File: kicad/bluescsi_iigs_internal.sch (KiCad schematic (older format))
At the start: 26 parts, among them J1 Conn_02x13_Odd_Even, J2 Conn_02x13_Odd_Even, J3 105162-0001, J4 Conn_01x02_Male, J5 Conn_01x02_Male, M1 Screw_Terminal_01x01, M2 Screw_Terminal_01x01, SW1 SW_SPDT, U1 YAAJ_BluePill, U2 UC560x, UCC56xx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

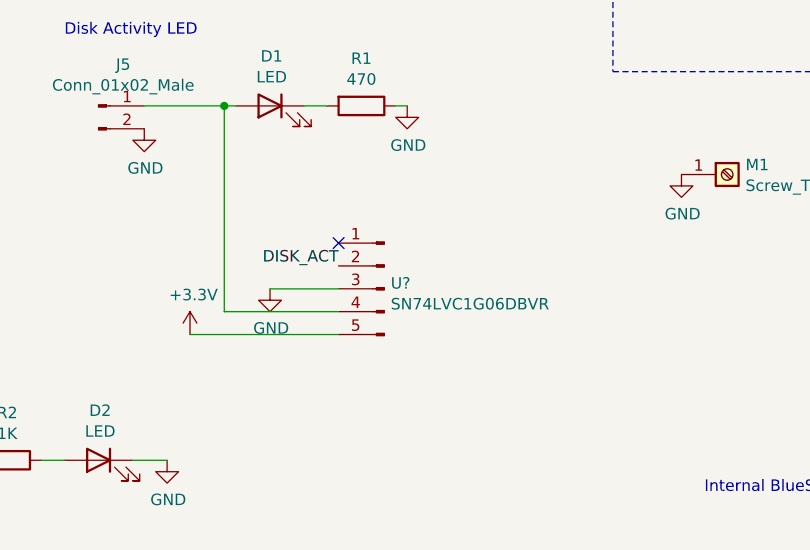
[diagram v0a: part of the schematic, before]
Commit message: Change regulator to back side tab up
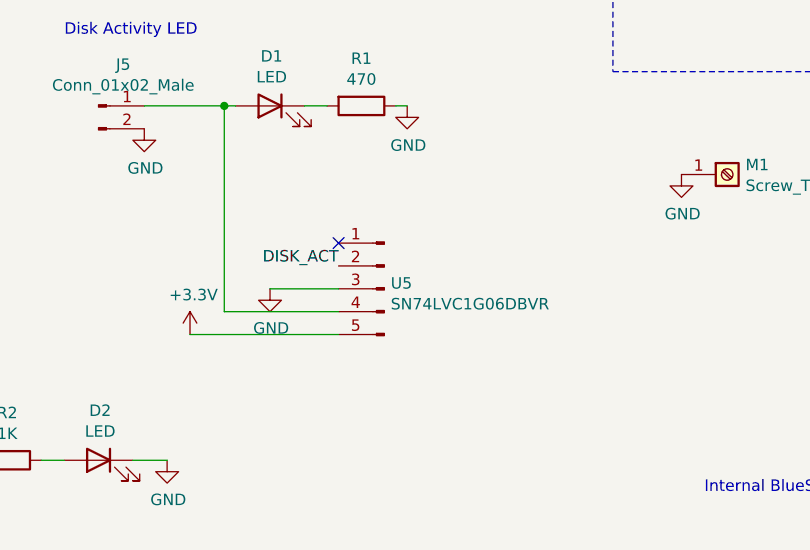
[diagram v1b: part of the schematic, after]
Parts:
- U4: footprint Package_TO_SOT_THT:TO-220-3_Vertical -> Package_TO_SOT_THT:TO-220-3_Horizontal_TabUp
- gave numbers to parts that had none: 1
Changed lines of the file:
@@
 F 0 "U4" H 9300 4842 50  0000 C CNN
 F 1 "MC7805CT-BP" H 9300 4751 50  0000 C CNN
-F 2 "Package_TO_SOT_THT:TO-220-3_Vertical" H 9300 4800 50  0001 C CNN
+F 2 "Package_TO_SOT_THT:TO-220-3_Horizontal_TabUp" H 9300 4800 50  0001 C CNN
 F 3 "https://www.mouser.com/datasheet/2/258/MC7805CT(TO-220)-E-1626349.pdf" H 9400 4350 50  0001 C CNN
 	1    9300 4600
@@
 $EndComp
 $Comp
-L Connector:Conn_01x05_Male U?
+L Connector:Conn_01x05_Male U5
 U 1 1 60C23A85
 P 5950 6600
-F 0 "U?" H 5922 6624 50  0000 R CNN
+F 0 "U5" H 5922 6624 50  0000 R CNN
 F 1 "SN74LVC1G06DBVR" H 5922 6533 50  0000 R CNN
 F 2 "Package_TO_SOT_SMD:SOT-23-5_HandSoldering" H 5950 6600 50  0001 C CNN
@@
 DISK_ACT
 $Comp
-L power:GND #PWR?
+L power:GND #PWR0126
 U 1 1 60C2A0B7
 P 5450 6600
-F 0 "#PWR?" H 5450 6350 50  0001 C CNN
+F 0 "#PWR0126" H 5450 6350 50  0001 C CNN
 F 1 "GND" H 5455 6427 50  0000 C CNN
 F 2 "" H 5450 6600 50  0001 C CNN
@@
 	5750 6600 5450 6600
 $Comp
-L power:+3.3V #PWR?
+L power:+3.3V #PWR0131
 U 1 1 60C2CD62
 P 5100 6800
-F 0 "#PWR?" H 5100 6650 50  0001 C CNN
+F 0 "#PWR0131" H 5100 6650 50  0001 C CNN
 F 1 "+3.3V" H 5115 6973 50  0000 C CNN
 F 2 "" H 5100 6800 50  0001 C CNN

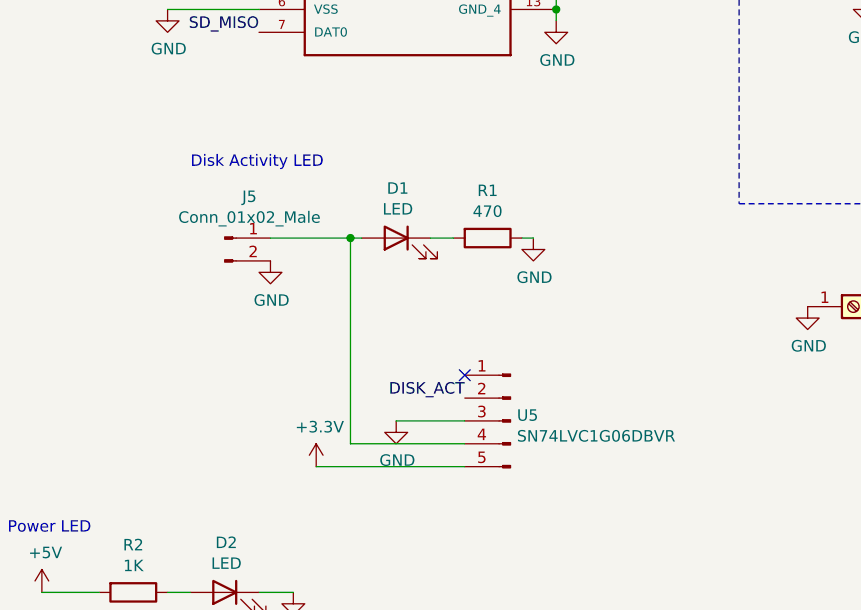
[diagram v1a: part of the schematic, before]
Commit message: Correct LED wiring for active-low with buffer IC
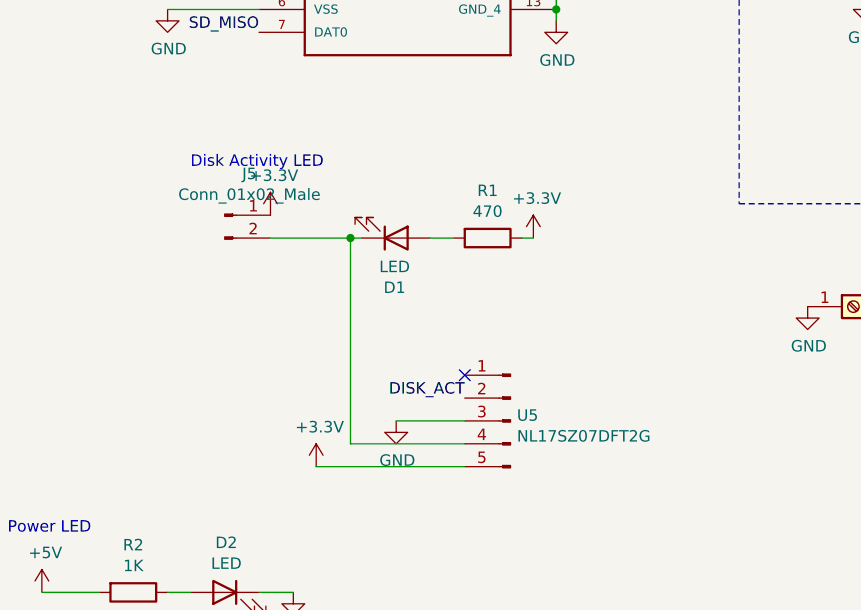
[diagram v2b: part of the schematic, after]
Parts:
- U5: value SN74LVC1G06DBVR -> NL17SZ07DFT2G; footprint Package_TO_SOT_SMD:SOT-23-5_HandSoldering -> Package_TO_SOT_SMD:SOT-353_SC-70-5_Handsoldering
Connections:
- net +3V3: now also J5.1 (Pin_1), R1.1
- net GND: no longer J5.2 (Pin_2), R1.1
- net at D1.1 (K): now also J5.2 (Pin_2), U5.4 (Pin_4); no longer R1.2
- new net: D1.2 (A), R1.2
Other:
- moved on the sheet: D1, J5
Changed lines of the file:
@@
 Wire Wire Line
 	5600 5800 5700 5800
-$Comp
-L power:GND #PWR0127
-U 1 1 609F55CD
-P 6050 5800
-F 0 "#PWR0127" H 6050 5550 50  0001 C CNN
-F 1 "GND" H 6055 5627 50  0000 C CNN
-F 2 "" H 6050 5800 50  0001 C CNN
-F 3 "" H 6050 5800 50  0001 C CNN
-	1    6050 5800
-	1    0    0    -1
-$EndComp
 Wire Wire Line
 	6000 5800 6050 5800
-$Comp
-L Connector:Conn_01x02_Male J5
-U 1 1 60AA760E
-P 4700 5800
-F 0 "J5" H 4808 5981 50  0000 C CNN
-F 1 "Conn_01x02_Male" H 4808 5890 50  0000 C CNN
-F 2 "Connector_PinHeader_2.54mm:PinHeader_1x02_P2.54mm_Vertical" H 4700 5800 50  0001 C CNN
-F 3 "~" H 4700 5800 50  0001 C CNN
-	1    4700 5800
-	1    0    0    -1
-$EndComp
-$Comp
-L power:GND #PWR0128
-U 1 1 60AA99DB
-P 4900 5900
-F 0 "#PWR0128" H 4900 5650 50  0001 C CNN
-F 1 "GND" H 4905 5727 50  0000 C CNN
-F 2 "" H 4900 5900 50  0001 C CNN
-F 3 "" H 4900 5900 50  0001 C CNN
-	1    4900 5900
-	1    0    0    -1
-$EndComp
 $Comp
 L power:GND #PWR0130
@@
 P 5950 6600
 F 0 "U5" H 5922 6624 50  0000 R CNN
-F 1 "SN74LVC1G06DBVR" H 5922 6533 50  0000 R CNN
-F 2 "Package_TO_SOT_SMD:SOT-23-5_HandSoldering" H 5950 6600 50  0001 C CNN
+F 1 "NL17SZ07DFT2G" H 5922 6533 50  0000 R CNN
+F 2 "Package_TO_SOT_SMD:SOT-353_SC-70-5_Handsoldering" H 5950 6600 50  0001 C CNN
 F 3 "https://www.mouser.com/datasheet/2/308/1/NL17SZ07_D-2318022.pdf" H 5950 6600 50  0001 C CNN
 	1    5950 6600
@@
 F 3 "~" H 5450 5800 50  0001 C CNN
 	1    5450 5800
-	-1   0    0    -1
+	1    0    0    1
+$EndComp
+$Comp
+L power:+3.3V #PWR0127
+U 1 1 60C2921C
+P 6050 5800
+F 0 "#PWR0127" H 6050 5650 50  0001 C CNN
+F 1 "+3.3V" H 6065 5973 50  0000 C CNN
+F 2 "" H 6050 5800 50  0001 C CNN
+F 3 "" H 6050 5800 50  0001 C CNN
+	1    6050 5800
+	1    0    0    -1
+$EndComp
+$Comp
+L Connector:Conn_01x02_Male J5
+U 1 1 60AA760E
+P 4700 5700
+F 0 "J5" H 4808 5881 50  0000 C CNN
+F 1 "Conn_01x02_Male" H 4808 5790 50  0000 C CNN
+F 2 "Connector_PinHeader_2.54mm:PinHeader_1x02_P2.54mm_Vertical" H 4700 5700 50  0001 C CNN
+F 3 "~" H 4700 5700 50  0001 C CNN
+	1    4700 5700
+	1    0    0    -1
+$EndComp
+$Comp
+L power:+3.3V #PWR0128
+U 1 1 60C2D753
+P 4900 5700
+F 0 "#PWR0128" H 4900 5550 50  0001 C CNN
+F 1 "+3.3V" H 4915 5873 50  0000 C CNN
+F 2 "" H 4900 5700 50  0001 C CNN
+F 3 "" H 4900 5700 50  0001 C CNN
+	1    4900 5700
+	1    0    0    -1
 $EndComp
 $EndSCHEMATC

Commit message: Added schematic for v1.3 (non-final), removed rendered board pictures not that we have REAL pictureds
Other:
- note added: "BlueGS"
- note added: "BlueGS: Internal BlueSCSI for Apple IIgs and //e"
- note added: "Mounting screws: Keystone 7774"
- note added: "https://github.com/xunker/blue-gs"
- note added: "v1.3 (non-final)"
- note removed: "Internal BlueSCSI for Apple IIgs and //e"
- note removed: "v1.2"
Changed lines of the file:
@@
 TERM_DIS
 Text Notes 7350 7500 0    50   ~ 0
-Internal BlueSCSI for Apple IIgs and //e
+BlueGS: Internal BlueSCSI for Apple IIgs and //e
 Text Notes 10600 7650 0    50   ~ 0
-v1.2
+v1.3 (non-final)
 Text Notes 3300 850  0    50   ~ 0
 Termination ICs\n\nCompatible ICs:\nUC5603, UC5604, UC5605, UCC5606, UCC5612, UCC5614
@@
 	0    1    1    0
 $EndComp
-Text Notes 4550 5500 0    50   ~ 0
+Text Notes 4400 5450 0    50   ~ 0
 Disk Activity LED
 Wire Notes Line
@@
 	1    0    0    -1
 $EndComp
+Text Notes 550  650  0    100  ~ 0
+BlueGS
+Text Notes 600  750  0    50   ~ 0
+https://github.com/xunker/blue-gs
+Text Notes 7100 5950 0    50   ~ 0
+Mounting screws: Keystone 7774
+Wire Notes Line
+	7050 5850 7050 6350
+Wire Notes Line
+	7050 6350 9850 6350
+Wire Notes Line
+	9850 6350 9850 5850
+Wire Notes Line
+	9850 5850 7050 5850
 $EndSCHEMATC

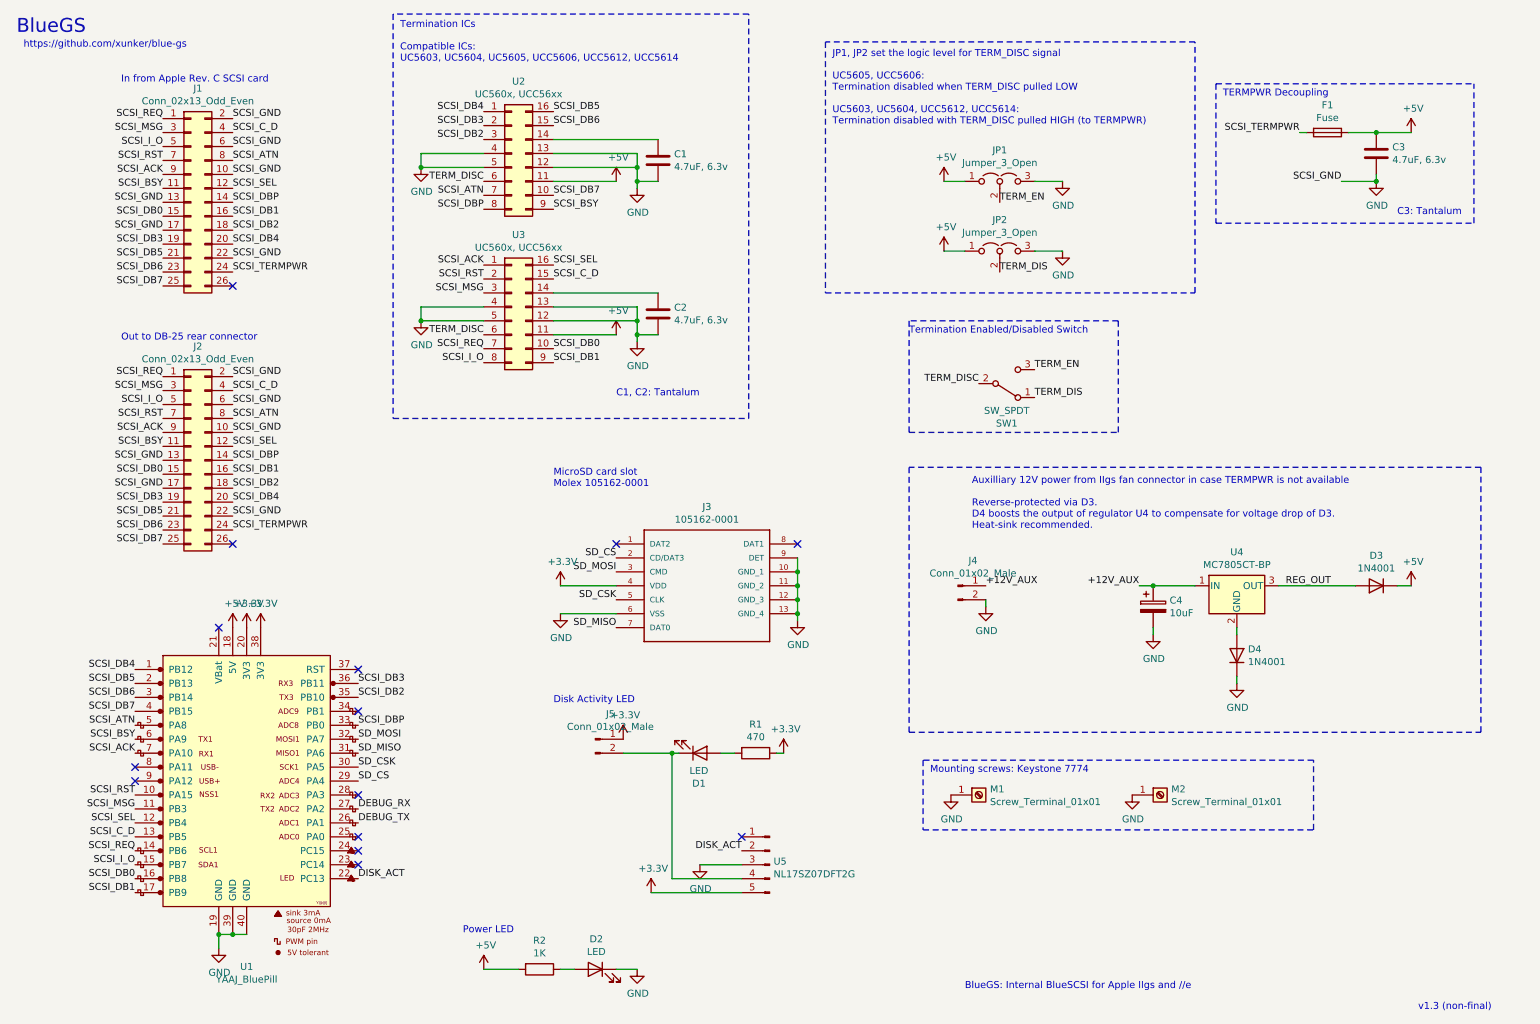
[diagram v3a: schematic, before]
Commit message: Add edge-mount db-25-m for scsi cards with fixed cables
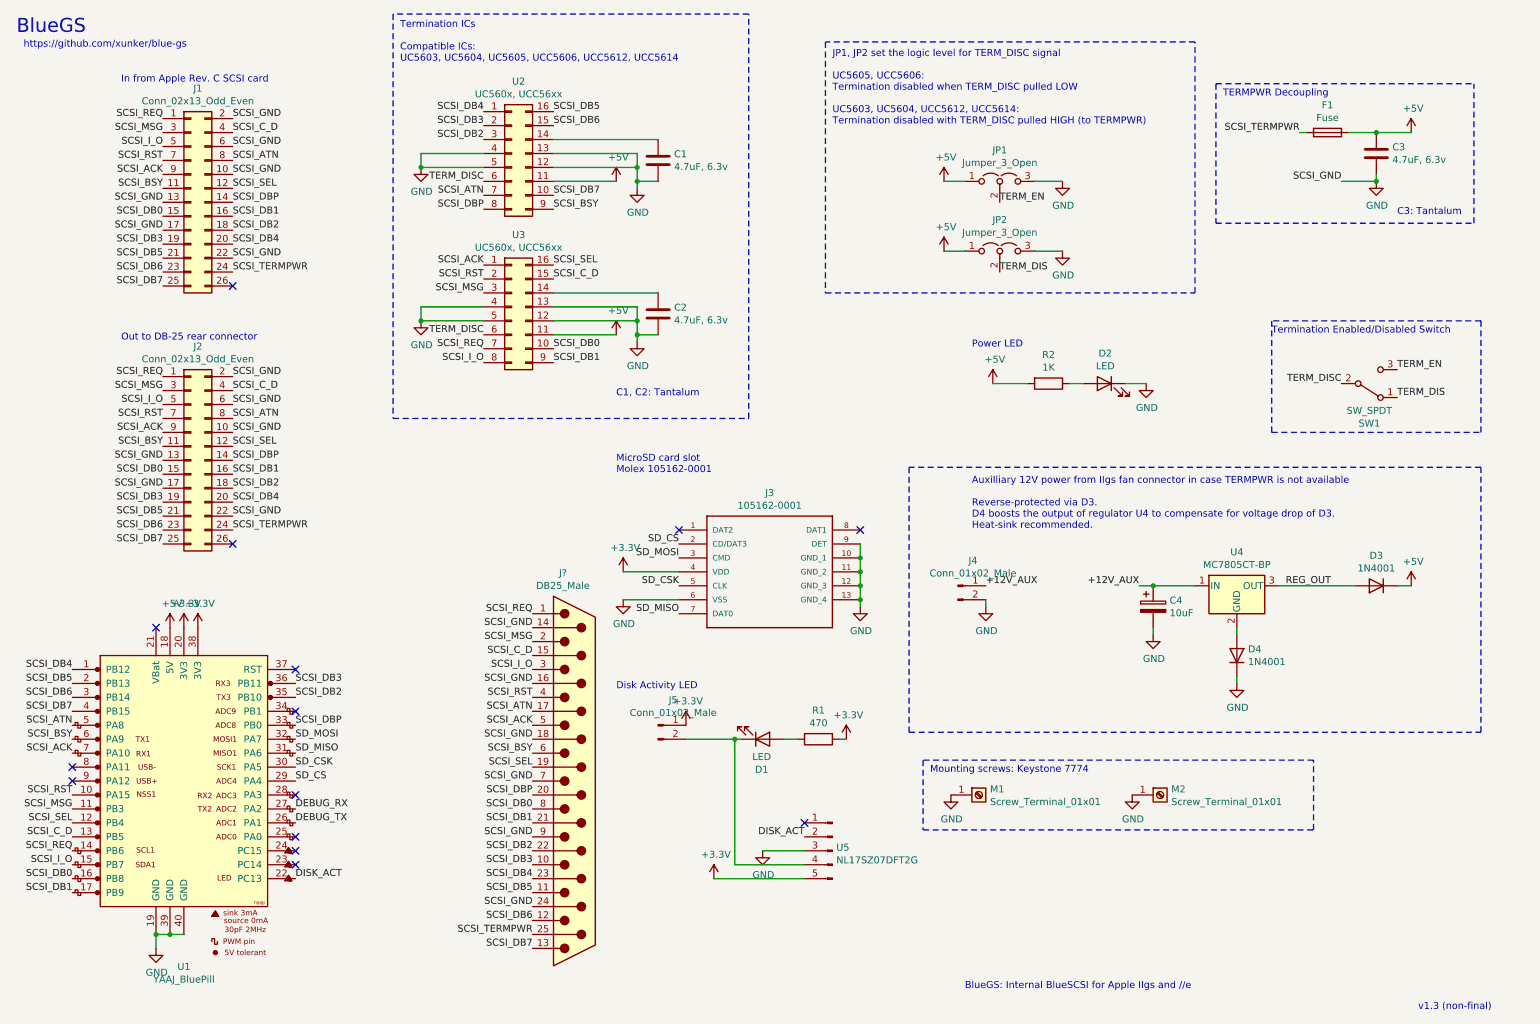
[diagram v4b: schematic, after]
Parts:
- added J?: DB25_Male, Connector_Dsub:DSUB-25_Male_EdgeMount_P2.77mm, symbol Connector:DB25_Male
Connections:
- net GND: now also J?.14 (P14), J?.16 (P16), J?.18 (P18), J?.24 (P24), J?.7, J?.9
- net SCSI_ACK: now also J?.5
- net SCSI_ATN: now also J?.17 (P17)
- net SCSI_BSY: now also J?.6
- net SCSI_C_D: now also J?.15 (P15)
- net SCSI_DB0: now also J?.8
- net SCSI_DB1: now also J?.21 (P21)
- net SCSI_DB2: now also J?.22 (P22)
- net SCSI_DB3: now also J?.10
- net SCSI_DB4: now also J?.23 (P23)
- net SCSI_DB5: now also J?.11
- net SCSI_DB6: now also J?.12
- net SCSI_DB7: now also J?.13
- net SCSI_DBP: now also J?.20 (P20)
- net SCSI_I_O: now also J?.3
- net SCSI_MSG: now also J?.2
- net SCSI_REQ: now also J?.1
- net SCSI_RST: now also J?.4
- net SCSI_SEL: now also J?.19 (P19)
- net SCSI_TERMPWR: now also J?.25 (P25)
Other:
- moved on the sheet: D1, D2, J3, J5, R1, R2, SW1, U1, U5

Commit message: Re-annotate schematic for connectors add SN field
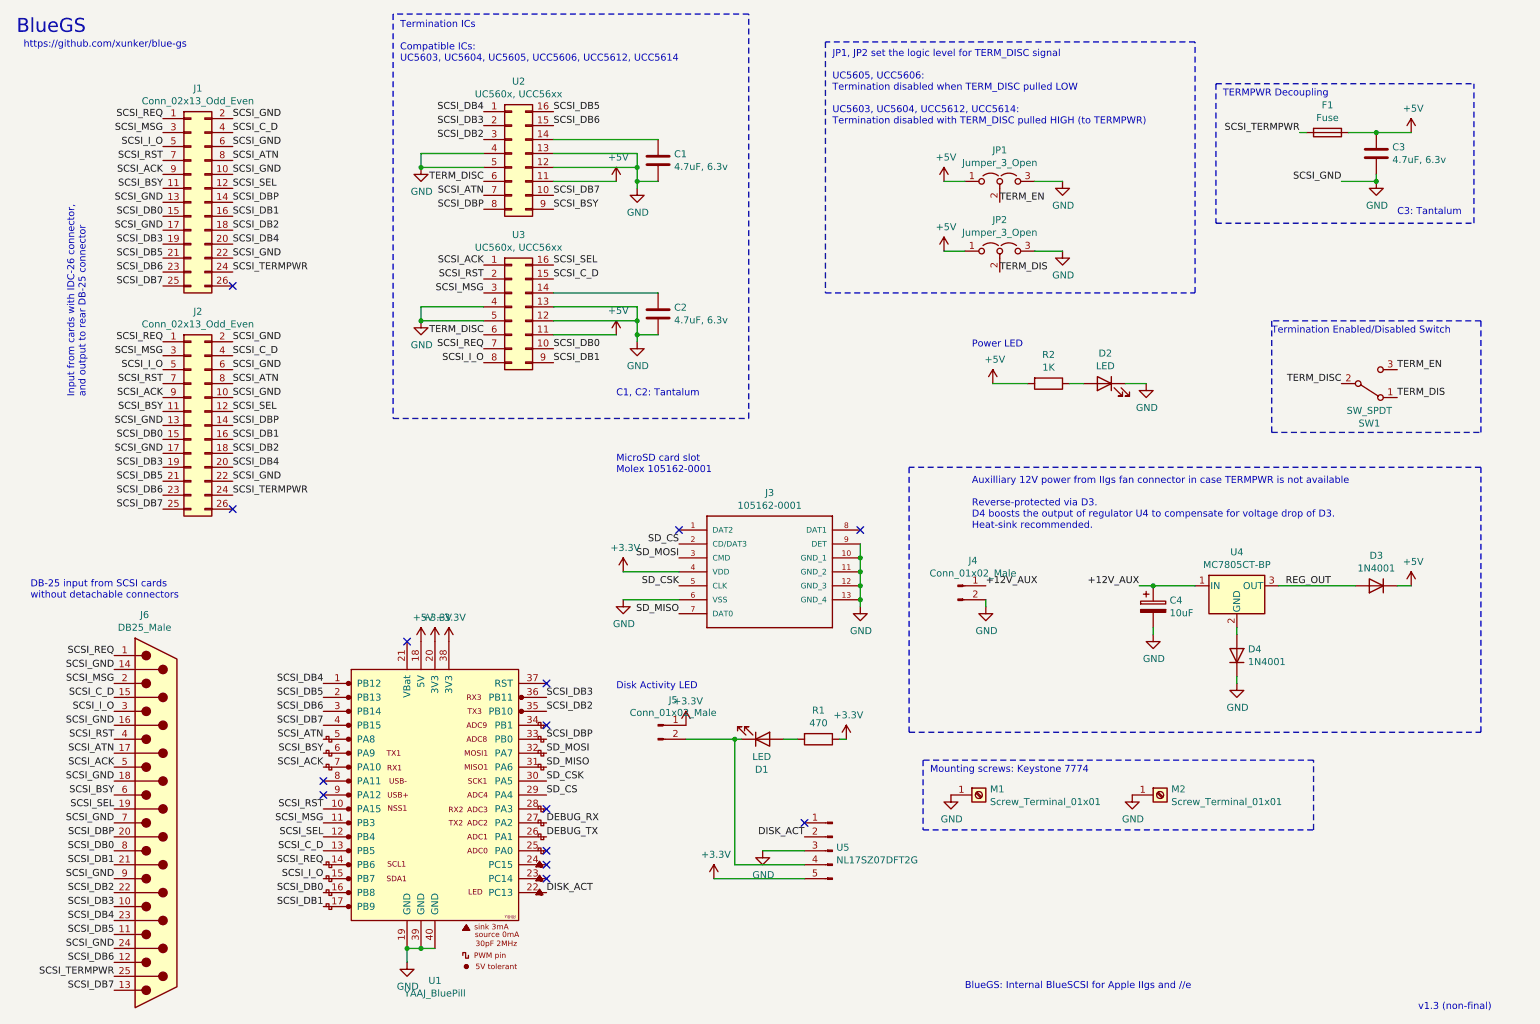
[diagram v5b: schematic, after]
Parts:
- gave numbers to parts that had none: 1
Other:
- note added: "DB-25 input from SCSI cards\nwithout detachable connectors"
- note added: "Input from cards with IDC-26 connector,\nand output to rear DB-25 connector"
- note removed: "In from Apple Rev. C SCSI card"
- note removed: "Out to DB-25 rear connector"
- moved on the sheet: J2, J6, U1
